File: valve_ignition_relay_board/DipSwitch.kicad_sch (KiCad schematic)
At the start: 7 parts, among them SW1 SW_DIP_x06

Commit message: Valve Ignition Relay - ready for review 1
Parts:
- SW1: footprint (none) -> Button_Switch_THT:SW_DIP_SPSTx06_Slide_9.78x17.42mm_W7.62mm_P2.54mm
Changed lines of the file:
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@@
 			)
 		)
-		(property "Footprint" ""
+		(property "Footprint" "Button_Switch_THT:SW_DIP_SPSTx06_Slide_9.78x17.42mm_W7.62mm_P2.54mm"
 			(at 123.19 91.44 0)
 			(effects

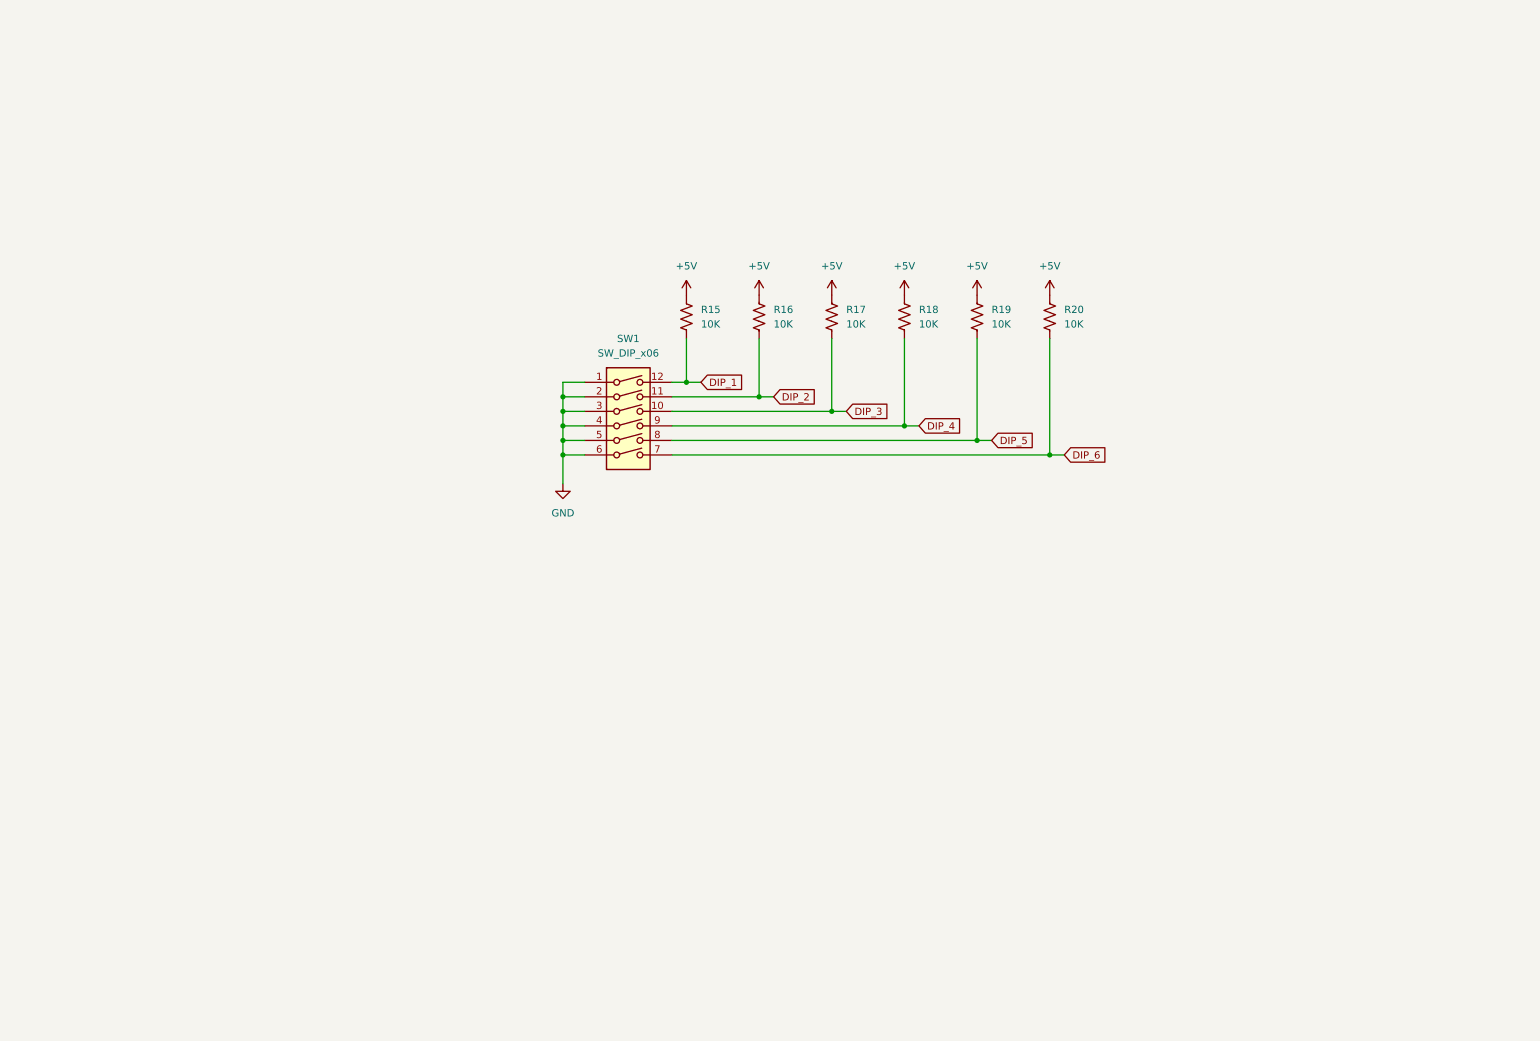
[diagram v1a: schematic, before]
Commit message: Added 4 new signals to the microcontroller
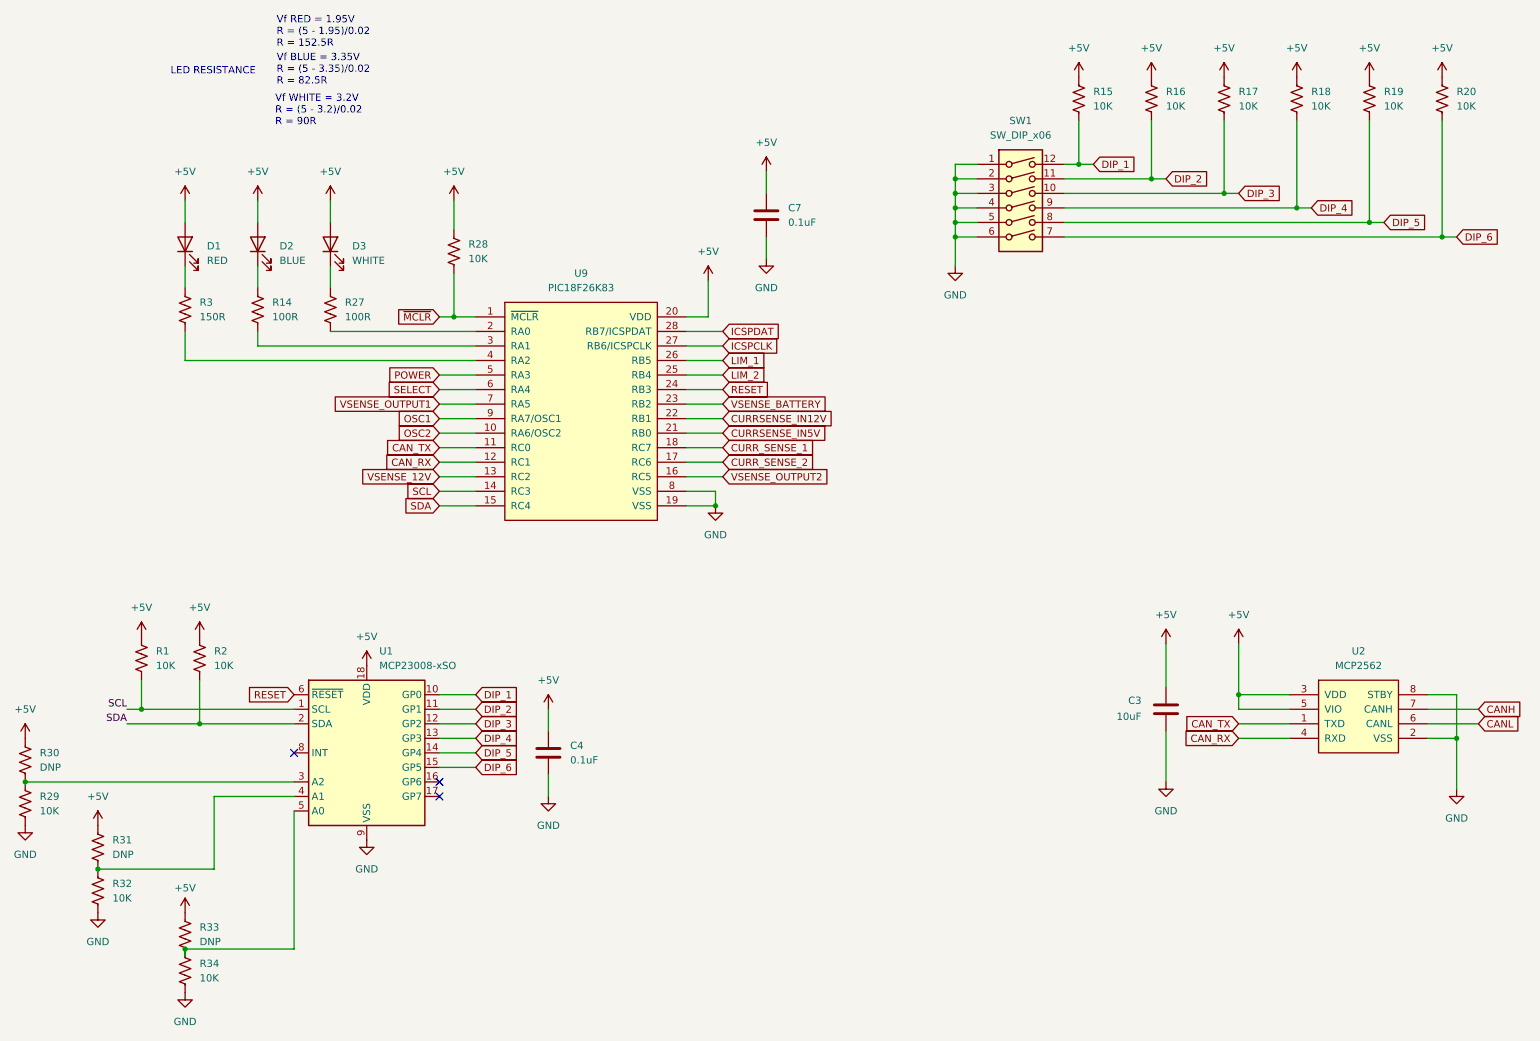
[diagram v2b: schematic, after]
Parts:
- added C3: 10uF, Capacitor_SMD:C_0805_2012Metric_Pad1.18x1.45mm_HandSolder, symbol Device:C
- added C4, C7: 0.1uF, Capacitor_SMD:C_0805_2012Metric_Pad1.18x1.45mm_HandSolder, symbol Device:C
- added D1: RED, LED_SMD:LED_1206_3216Metric_Pad1.42x1.75mm_HandSolder, symbol Device:LED
- added D2: BLUE, LED_SMD:LED_1206_3216Metric_Pad1.42x1.75mm_HandSolder, symbol Device:LED
- added D3: WHITE, LED_SMD:LED_1206_3216Metric_Pad1.42x1.75mm_HandSolder, symbol Device:LED
- added R1, R2, R28, R29, R32, R34: 10K, Resistor_SMD:R_0805_2012Metric_Pad1.20x1.40mm_HandSolder, symbol Device:R_US
- added R14, R27: 100R, Resistor_SMD:R_0805_2012Metric_Pad1.20x1.40mm_HandSolder, symbol Device:R_US
- added R3: 150R, Resistor_SMD:R_0805_2012Metric_Pad1.20x1.40mm_HandSolder, symbol Device:R_US
- added R30, R31, R33: DNP, Resistor_SMD:R_0805_2012Metric_Pad1.20x1.40mm_HandSolder, symbol Device:R_US
- added U1: MCP23008-xSO, Package_SO:SOIC-18W_7.5x11.6mm_P1.27mm, symbol Interface_Expansion:MCP23008-xSO
- added U2: MCP2562, Package_SO:SOIC-8_3.9x4.9mm_P1.27mm, symbol canhw:MCP2562
- added U9: PIC18F26K83, Package_SO:SOIC-28W_7.5x18.7mm_P1.27mm, symbol canhw:PIC18F26K83
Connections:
- net +5V: now also C3.1, C4.1, C7.1, D1.2 (A), D2.2 (A), D3.2 (A), R1.1, R2.1, R28.1, R30.1, R31.1, R33.1, U1.18 (VDD), U2.3 (VDD), U2.5 (VIO), U9.20 (VDD)
- net DIP_1: now also U1.10 (GP0)
- net DIP_2: now also U1.11 (GP1)
- net DIP_3: now also U1.12 (GP2)
- net DIP_4: now also U1.13 (GP3)
- net DIP_5: now also U1.14 (GP4)
- net DIP_6: now also U1.15 (GP5)
- net GND: now also C3.2, C4.2, C7.2, R29.2, R32.2, R34.2, U1.9 (VSS), U2.2 (VSS), U2.8 (STBY), U9.19 (VSS), U9.8 (VSS)
- new net: R33.2, R34.1, U1.5 (A0)
- new net: R29.1, R30.2, U1.3 (A2)
- new net: R31.2, R32.1, U1.4 (A1)
- new net: D1.1 (K), R3.1
- new net: D3.1 (K), R27.1
- new net: R27.2, U9.2 (RA0)
- new net: R14.2, U9.3 (RA1)
- new net: R3.2, U9.4 (RA2)
- new net: D2.1 (K), R14.1
- new net CANH: U2.7 (CANH)
- new net CANL: U2.6 (CANL)
- new net CAN_RX: U2.4 (RXD), U9.12 (RC1)
- new net CAN_TX: U2.1 (TXD), U9.11 (RC0)
- new net CURRSENSE_IN12V: U9.22 (RB1)
- new net CURRSENSE_IN5V: U9.21 (RB0)
- new net CURR_SENSE_1: U9.18 (RC7)
- new net CURR_SENSE_2: U9.17 (RC6)
- new net ICSPCLK: U9.27 (RB6/ICSPCLK)
- new net ICSPDAT: U9.28 (RB7/ICSPDAT)
- new net LIM_1: U9.26 (RB5)
- new net LIM_2: U9.25 (RB4)
- new net OSC1: U9.9 (RA7/OSC1)
- new net OSC2: U9.10 (RA6/OSC2)
- new net POWER: U9.5 (RA3)
- new net RESET: U1.6 (~{RESET}), U9.24 (RB3)
- new net SCL: R1.2, U1.1 (SCL), U9.14 (RC3)
- new net SDA: R2.2, U1.2 (SDA), U9.15 (RC4)
- new net SELECT: U9.6 (RA4)
- new net VSENSE_12V: U9.13 (RC2)
- new net VSENSE_BATTERY: U9.23 (RB2)
- new net VSENSE_OUTPUT1: U9.7 (RA5)
- new net VSENSE_OUTPUT2: U9.16 (RC5)
- new net ~{MCLR}: R28.2, U9.1 (~{MCLR})
- no-connect marks 0 -> 3
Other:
- note added: "LED RESISTANCE"
- note added: "Vf BLUE = 3.35V R = (5 - 3.35)/0.02 R = 82.5R"
- note added: "Vf RED = 1.95V R = (5 - 1.95)/0.02 R = 152.5R"
- note added: "Vf WHITE = 3.2V R = (5 - 3.2)/0.02 R = 90R"
- moved on the sheet: R15, R16, R17, R18, R19, R20, SW1
